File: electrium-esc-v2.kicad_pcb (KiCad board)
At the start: 2 copper layers, 45 x 55 mm, 72 parts, among them IC1 LMR36510FADDAR, J1 CAN, J2 USB_B_Micro, J3 GPIO, J4 Conn_01x02, J5 Debugger Pins, J6 3.3VJumper, Q1 IRF3205, Q2 IRF3205, Q3 IRF3205, Q4 IRF3205, Q5 IRF3205, Q6 IRF3205, U1 NCP1117-3.3_SOT223, U2 W25Q128JVS, U3 RP2040, U4 DRV8323HRTAR, U5 NRF24L01_Breakout, U6 SN65HVD233, Y1 ABLS-12.000MHZ-B4-T

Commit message: Add final pads
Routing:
- added copper zone on F.Cu, net /MOSFETs/SH1
- added copper zone on F.Cu, net /MOSFETs/SH2
- added copper zone on F.Cu, net /MOSFETs/SH3
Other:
- board text added: "P1"
- board text added: "P2"
- board text added: "P3"
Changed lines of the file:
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@@
     )
+    (stroke (width 0.1) (type solid)) (fill solid) (layer "F.Mask"))
+  (gr_rect (start 168.3004 96.139) (end 171.196 98.7298)
     (stroke (width 0.1) (type solid)) (fill solid) (layer "F.Mask"))
   (gr_rect (start 160.1724 87.884) (end 164.338 94.1832)
+    (stroke (width 0.1) (type solid)) (fill solid) (layer "F.Mask"))
+  (gr_rect (start 182.9816 96.0882) (end 185.8772 98.679)
     (stroke (width 0.1) (type solid)) (fill solid) (layer "F.Mask"))
   (gr_poly
@@
     )
     (stroke (width 0.1) (type solid)) (fill solid) (layer "F.Mask"))
+  (gr_rect (start 197.5612 96.0628) (end 200.4568 98.6536)
+    (stroke (width 0.1) (type solid)) (fill solid) (layer "F.Mask"))
   (gr_rect (start 160 43.84) (end 205 98.84)
     (stroke (width 0.2) (type default)) (fill none) (layer "Edge.Cuts"))
   (gr_text "Electrium Mobility ESC V2.0" (at 197.8152 82.3976) (layer "B.SilkS")
     (effects (font (size 1.5 1.5) (thickness 0.3) bold) (justify left bottom mirror))
+  )
+  (gr_text "P2\n" (at 186.2836 98.3996) (layer "F.SilkS")
+    (effects (font (size 1.5 1.5) (thickness 0.3) bold) (justify left bottom))
+  )
+  (gr_text "P3\n" (at 200.9648 98.3996) (layer "F.SilkS")
+    (effects (font (size 1.5 1.5) (thickness 0.3) bold) (justify left bottom))
+  )
+  (gr_text "P1" (at 171.5516 98.4504) (layer "F.SilkS")
+    (effects (font (size 1.5 1.5) (thickness 0.3) bold) (justify left bottom))
   )
   (gr_text "-\n" (at 159.9184 96.012) (layer "F.SilkS")
@@
   (segment (start 184.9628 59.8932) (end 184.4548 59.3852) (width 0.1778) (layer "B.Cu") (net 3))
   (segment (start 184.9628 60.9978) (end 184.9628 59.8932) (width 0.1778) (layer "B.Cu") (net 3))
-  (segment (start 186.5884 57.3532) (end 186.5884 57.5056) (width 0.1778) (layer "B.Cu") (net 3))
   (segment (start 183.2864 61.0108) (end 183.2864 60.5536) (width 0.1778) (layer "B.Cu") (net 3))
   (segment (start 185.0136 55.8292) (end 185.0644 55.8292) (width 0.1778) (layer "B.Cu") (net 3))
@@
     )
   )
+  (zone (net 43) (net_name "/MOSFETs/SH3") (layer "F.Cu") (hatch edge 0.5)
+    (priority 12)
+    (connect_pads yes (clearance 0))
+    (min_thickness 0.25) (filled_areas_thickness no)
+    (fill yes (thermal_gap 0.5) (thermal_bridge_width 0.5))
+    (polygon
+      (pts
+        (xy 197.5612 93.0148)
+        (xy 200.5076 92.964)
+        (xy 200.5076 98.6028)
+        (xy 197.5612 98.6536)
+      )
+    )
+  )
   (zone (net 1) (net_name "GND") (layer "F.Cu") (hatch edge 0.5)
     (priority 10)
@@
         (xy 160.1216 86.4108)
         (xy 166.624 86.4108)
+      )
+    )
+  )
+  (zone (net 41) (net_name "/MOSFETs/SH2") (layer "F.Cu") (hatch edge 0.5)
+    (priority 12)
+    (connect_pads yes (clearance 0))
+    (min_thickness 0.25) (filled_areas_thickness no)
+    (fill yes (thermal_gap 0.5) (thermal_bridge_width 0.5))
+    (polygon
+      (pts
+        (xy 182.9816 93.0402)
+        (xy 185.928 92.9894)
+        (xy 185.928 98.6282)
+        (xy 182.9816 98.679)
       )
     )
@@
     )
   )
+  (zone (net 39) (net_name "/MOSFETs/SH1") (layer "F.Cu") (hatch edge 0.5)
+    (priority 12)
+    (connect_pads yes (clearance 0))
+    (min_thickness 0.25) (filled_areas_thickness no)
+    (fill yes (thermal_gap 0.5) (thermal_bridge_width 0.5))
+    (polygon
+      (pts
+        (xy 168.3004 93.091)
+        (xy 171.2468 93.0402)
+        (xy 171.2468 98.679)
+        (xy 168.3004 98.7298)
+      )
+    )
+  )
   (zone (net 3) (net_name "+3.3V") (layer "F.Cu") (hatch edge 0.5)
     (priority 9)
@@
     (polygon
       (pts
-        (xy 204.978 103.8352)
+        (xy 205.0288 98.4504)
         (xy 204.978 43.8404)
         (xy 160.02 43.8404)
-        (xy 160.02 103.8352)
-      )
-    )
+        (xy 160.0708 98.4504)
+      )
+    )

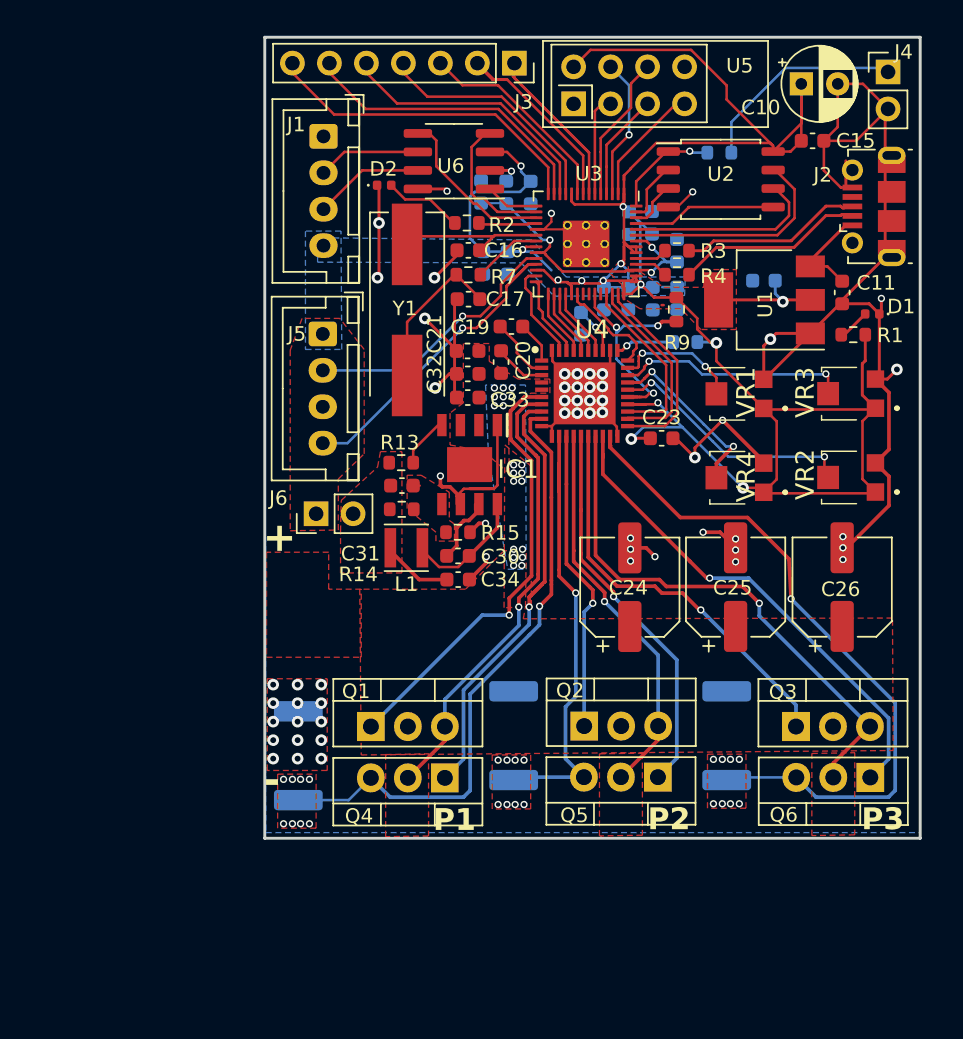
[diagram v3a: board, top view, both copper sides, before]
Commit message: Add better traces
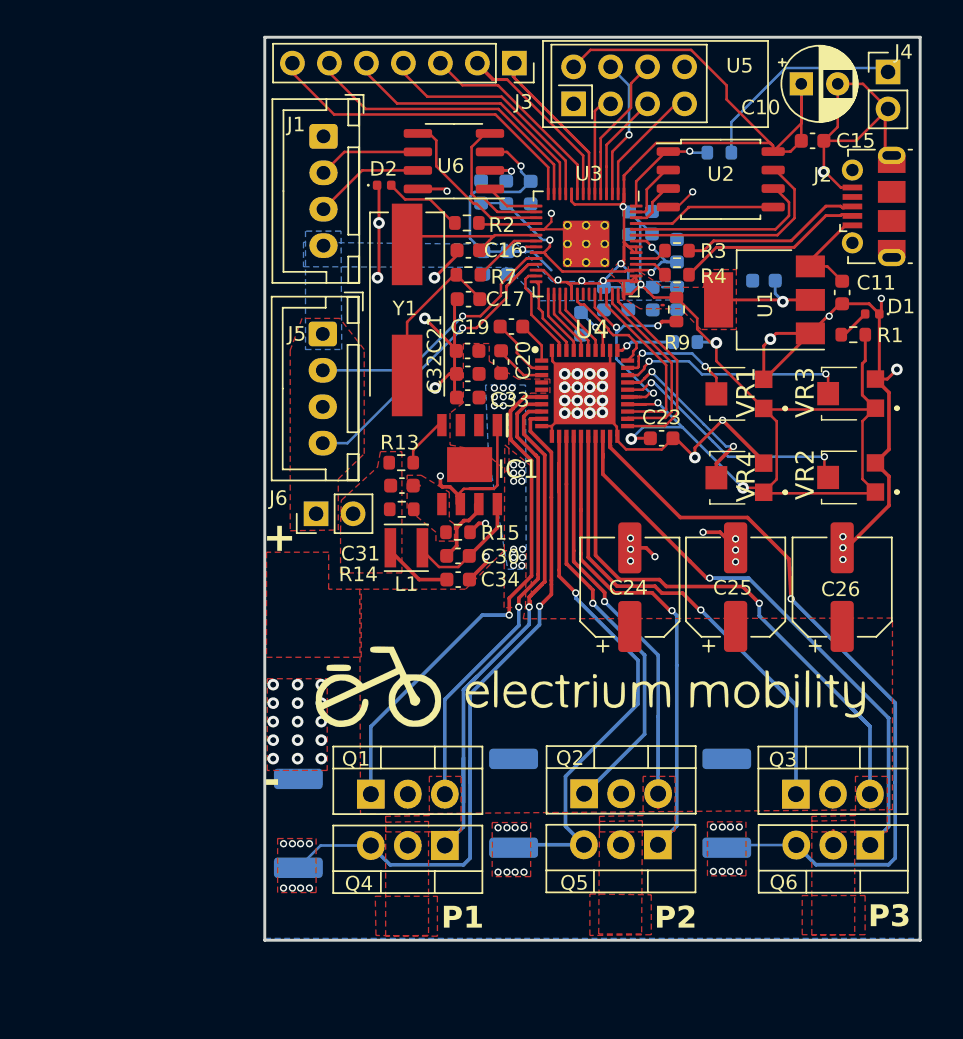
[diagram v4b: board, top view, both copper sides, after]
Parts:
- added G***: LOGO, LOGO, F.Cu at (183.0, 89.6)
- added G***: LOGO, LOGO, B.Cu at (182.1, 90.4)
- moved Q1 4.64 mm to (167.3, 95.8)
- moved Q2 4.64 mm to (181.9, 95.8)
- moved Q3 4.64 mm to (196.5, 95.8)
- moved Q4 4.64 mm to (172.4, 99.3)
- moved Q5 4.64 mm to (187.0, 99.3)
- moved Q6 4.64 mm to (201.6, 99.3)
- moved R10 4.64 mm to (162.3, 97.8)
- moved R11 4.64 mm to (177.1, 96.4)
- moved R12 4.64 mm to (191.7, 96.4)
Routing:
- net /MOSFETs/M_L1: track 30.8 -> 39.8 mm
- net /MOSFETs/SP2: track 31.7 -> 39.9 mm
- net GND: track 149.2 -> 141.0 mm, vias 83 -> 85
- net /MOSFETs/M_L2: track 20.9 -> 28.5 mm
- net /MOSFETs/M_H3: track 28.1 -> 34.9 mm
- net /MOSFETs/M_H2: track 26.7 -> 33.1 mm
- net /MOSFETs/SP1: track 42.4 -> 48.4 mm
- net /MOSFETs/M_L3: track 34.0 -> 38.6 mm
- net /MOSFETs/M_H1: track 30.5 -> 35.2 mm
- net /MOSFETs/SP3: track 48.7 -> 53.3 mm
- net /MOSFETs/SH3: track 36.9 -> 39.9 mm
- net /MOSFETs/SH2: track 26.9 -> 27.9 mm
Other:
- board size 45 x 55 mm -> 45 x 62 mm
- board text added: "ESC V2.0"
- board text removed: "Electrium Mobility ESC V2.0"

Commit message: Fix traces
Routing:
- net GND: track 141.0 -> 94.9 mm, vias 85 -> 88
- net +3.3V: track 181.6 -> 182.4 mm

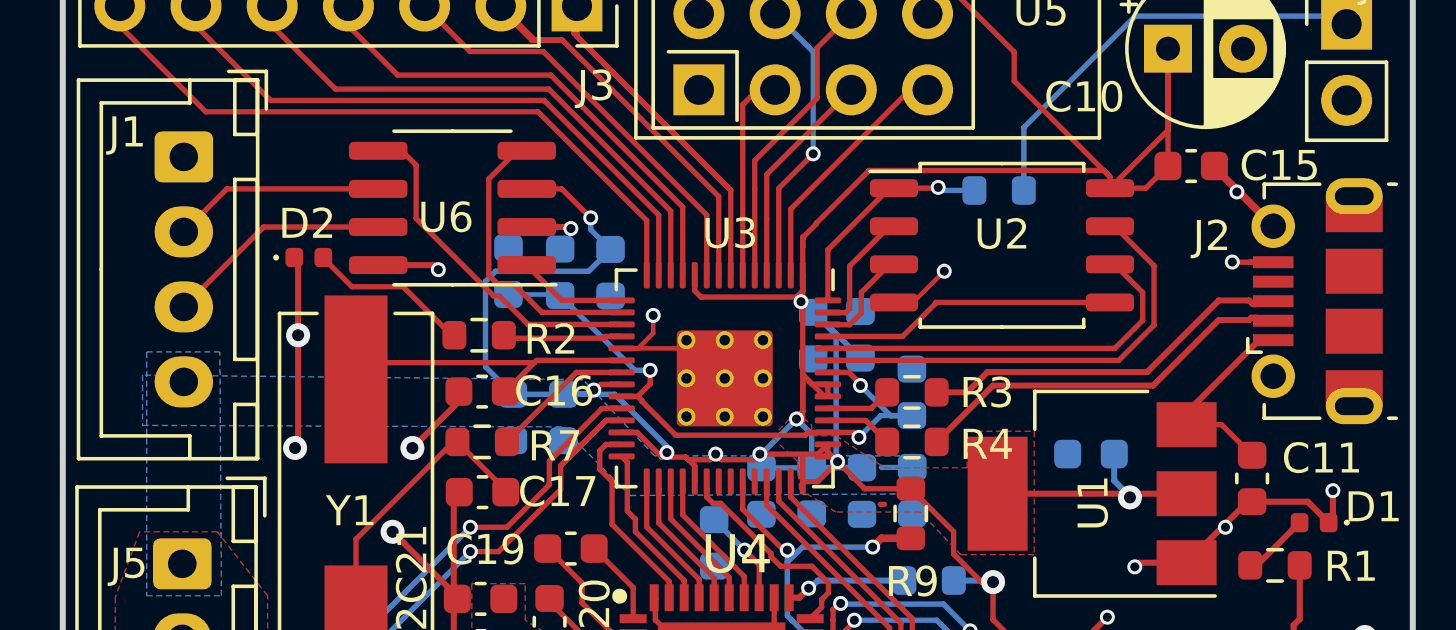
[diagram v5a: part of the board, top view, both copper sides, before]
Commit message: Add CAN bus thicker traces
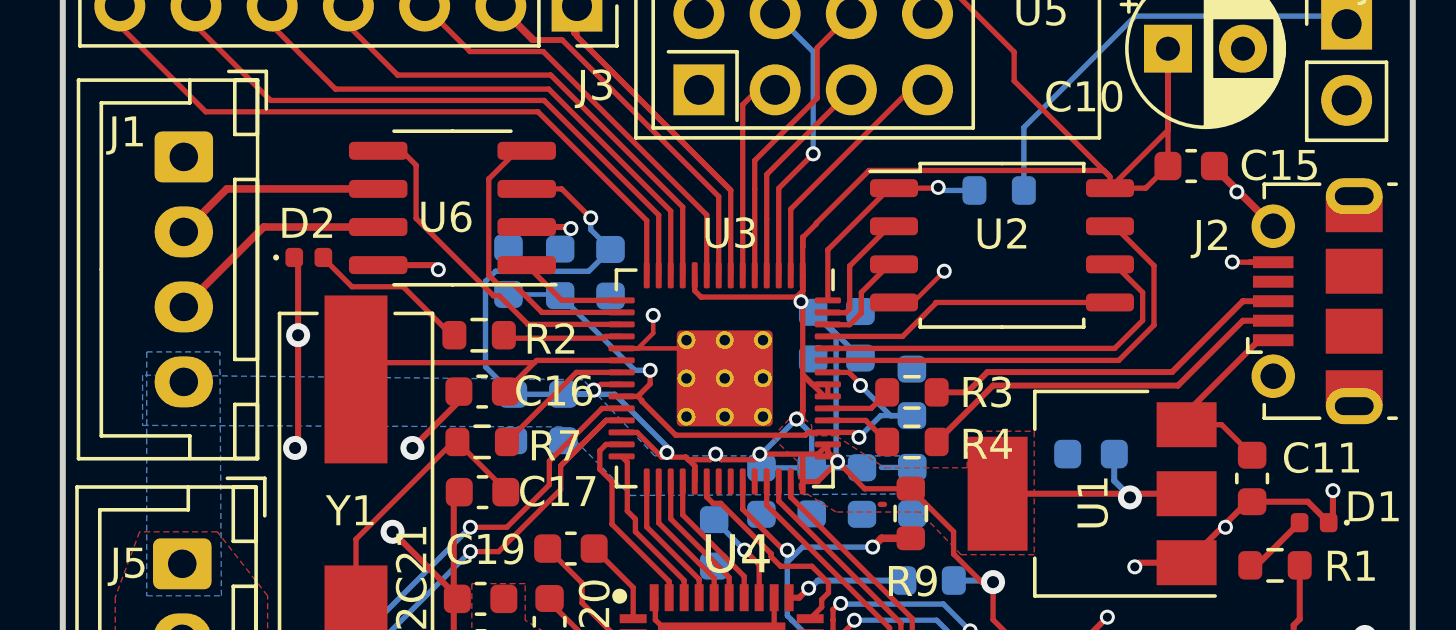
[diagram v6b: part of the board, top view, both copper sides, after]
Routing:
- net /MCU/USB_D-: track 13.0 -> 13.5 mm
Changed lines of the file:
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@@
   (segment (start 170.1922 72.1862) (end 171.9072 70.4712) (width 0.1778) (layer "F.Cu") (net 14))
   (segment (start 170.1922 73.0504) (end 170.1922 72.1862) (width 0.1778) (layer "F.Cu") (net 14))
-  (segment (start 165.4664 51.7144) (end 170.5132 51.7144) (width 0.1778) (layer "F.Cu") (net 16))
-  (segment (start 164.0332 53.1476) (end 165.4664 51.7144) (width 0.1778) (layer "F.Cu") (net 16))
-  (segment (start 170.5132 52.9844) (end 166.6964 52.9844) (width 0.1778) (layer "F.Cu") (net 17))
-  (segment (start 166.6964 52.9844) (end 164.0332 55.6476) (width 0.1778) (layer "F.Cu") (net 17))
+  (segment (start 170.5132 51.7144) (end 165.4664 51.7144) (width 0.254) (layer "F.Cu") (net 16))
+  (segment (start 165.4664 51.7144) (end 164.0332 53.1476) (width 0.254) (layer "F.Cu") (net 16))
+  (segment (start 170.5132 52.9844) (end 166.6964 52.9844) (width 0.254) (layer "F.Cu") (net 17))
+  (segment (start 166.6964 52.9844) (end 164.0332 55.6476) (width 0.254) (layer "F.Cu") (net 17))
   (segment (start 187.4784 58.4962) (end 186.9441 59.0305) (width 0.1778) (layer "F.Cu") (net 18))
   (segment (start 186.9441 59.0305) (end 185.5015 59.0305) (width 0.1778) (layer "F.Cu") (net 18))
@@
   (segment (start 169.7736 63.389348) (end 169.7736 67.0644) (width 0.1778) (layer "F.Cu") (net 24))
   (segment (start 170.1938 74.6252) (end 170.6372 74.6252) (width 0.1778) (layer "F.Cu") (net 25))
-  (segment (start 199.5424 56.0836) (end 198.529899 56.0836) (width 0.2) (layer "F.Cu") (net 26))
-  (segment (start 191.006219 58.269381) (end 189.1284 60.1472) (width 0.2) (layer "F.Cu") (net 26))
   (segment (start 199.8726 56.1076) (end 199.7726 56.0076) (width 0.2) (layer "F.Cu") (net 26))
-  (segment (start 199.7726 56.0076) (end 199.6184 56.0076) (width 0.2) (layer "F.Cu") (net 26))
+  (segment (start 199.335099 56.1076) (end 200.3476 56.1076) (width 0.2) (layer "F.Cu") (net 26))
+  (segment (start 189.1284 60.1472) (end 191.006219 58.269381) (width 0.2) (layer "F.Cu") (net 26))
   (segment (start 200.3476 56.1076) (end 199.8726 56.1076) (width 0.2) (layer "F.Cu") (net 26))
-  (segment (start 198.529899 56.0836) (end 196.344118 58.269381) (width 0.2) (layer "F.Cu") (net 26))
-  (segment (start 199.6184 56.0076) (end 199.5424 56.0836) (width 0.2) (layer "F.Cu") (net 26))
-  (segment (start 196.344118 58.269381) (end 191.006219 58.269381) (width 0.2) (layer "F.Cu") (net 26))
-  (segment (start 199.6664 55.5576) (end 199.5424 55.4336) (width 0.2) (layer "F.Cu") (net 27))
+  (segment (start 191.006219 58.269381) (end 197.173318 58.269381) (width 0.2) (layer "F.Cu") (net 26))
+  (segment (start 197.173318 58.269381) (end 199.335099 56.1076) (width 0.2) (layer "F.Cu") (net 26))
+  (segment (start 190.819803 57.8194) (end 196.973299 57.8194) (width 0.2) (layer "F.Cu") (net 27))
+  (segment (start 199.335099 55.4576) (end 200.3476 55.4576) (width 0.2) (layer "F.Cu") (net 27))
+  (segment (start 190.143003 58.4962) (end 190.819803 57.8194) (width 0.2) (layer "F.Cu") (net 27))
+  (segment (start 200.3476 55.4576) (end 199.8726 55.4576) (width 0.2) (layer "F.Cu") (net 27))
   (segment (start 189.1284 58.4962) (end 190.143003 58.4962) (width 0.2) (layer "F.Cu") (net 27))
-  (segment (start 198.529899 55.4336) (end 199.5424 55.4336) (width 0.2) (layer "F.Cu") (net 27))
-  (segment (start 200.3476 55.4576) (end 199.8726 55.4576) (width 0.2) (layer "F.Cu") (net 27))
-  (segment (start 190.819803 57.8194) (end 196.144099 57.8194) (width 0.2) (layer "F.Cu") (net 27))
-  (segment (start 196.144099 57.8194) (end 198.529899 55.4336) (width 0.2) (layer "F.Cu") (net 27))
-  (segment (start 190.143003 58.4962) (end 190.819803 57.8194) (width 0.2) (layer "F.Cu") (net 27))
-  (segment (start 199.8726 55.4576) (end 199.7726 55.5576) (width 0.2) (layer "F.Cu") (net 27))
-  (segment (start 199.7726 55.5576) (end 199.6664 55.5576) (width 0.2) (layer "F.Cu") (net 27))
+  (segment (start 196.973299 57.8194) (end 199.335099 55.4576) (width 0.2) (layer "F.Cu") (net 27))
   (segment (start 179.464 54.593) (end 179.464 52.7688) (width 0.1778) (layer "F.Cu") (net 29))
   (segment (start 179.464 52.7688) (end 175.83869 49.14349) (width 0.1778) (layer "F.Cu") (net 29))

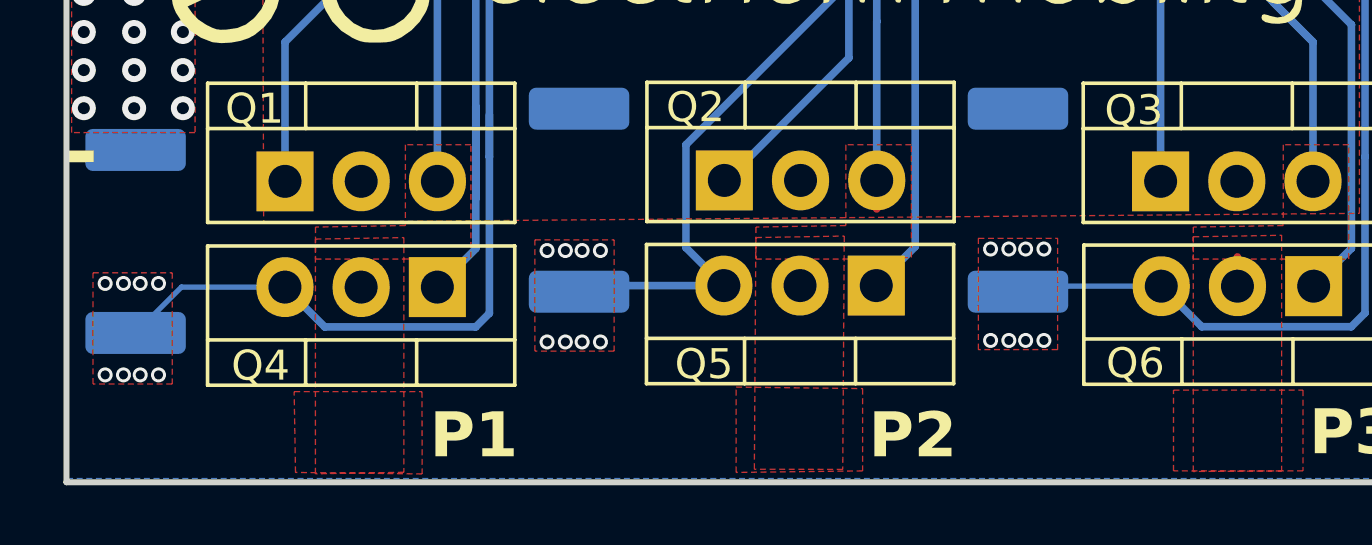
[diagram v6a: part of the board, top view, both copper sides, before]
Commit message: Add more trace width
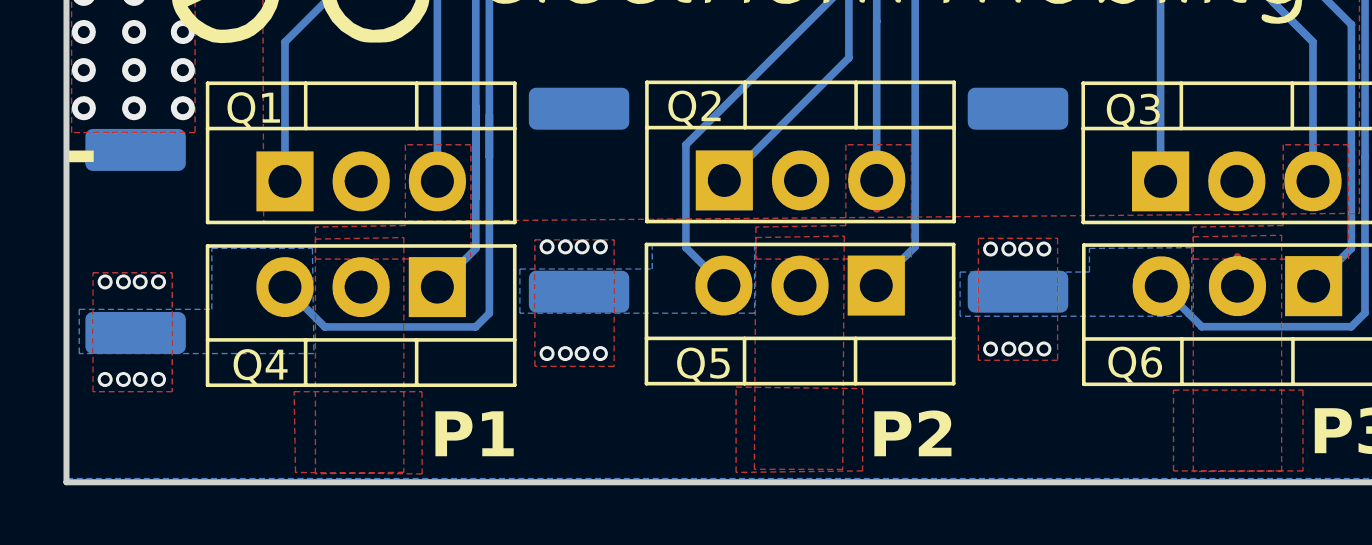
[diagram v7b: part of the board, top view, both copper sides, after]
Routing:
- net /MOSFETs/SP1: track 48.4 -> 42.8 mm
- net /MOSFETs/SP2: track 39.9 -> 35.3 mm
- net /MOSFETs/SP3: track 53.3 -> 48.7 mm
- added copper zone on B.Cu, net /MOSFETs/SP1
- added copper zone on B.Cu, net /MOSFETs/SP2
- added copper zone on B.Cu, net /MOSFETs/SP3
